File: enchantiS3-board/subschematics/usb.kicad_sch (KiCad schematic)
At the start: 3 parts, among them J1 USB_C_Receptacle_USB2.0, U1 USBLC6-2P6

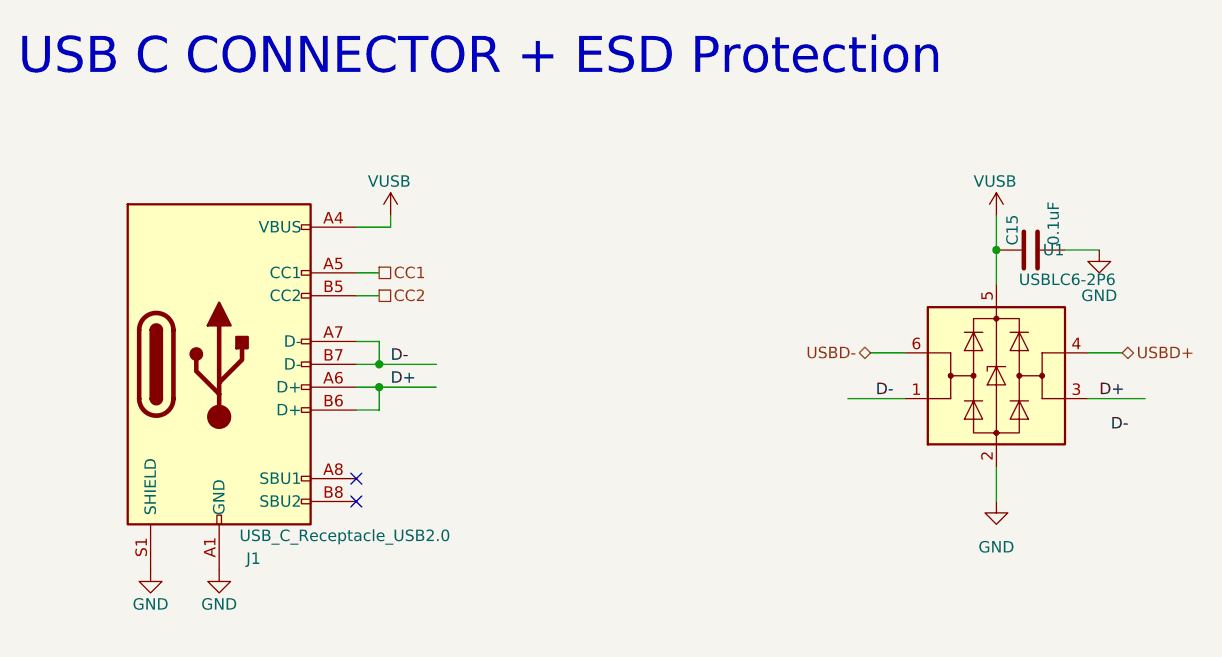
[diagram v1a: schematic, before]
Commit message: Added circuit for magnetometer, added circuit for canfd transceiver, updated circuit for USB connector
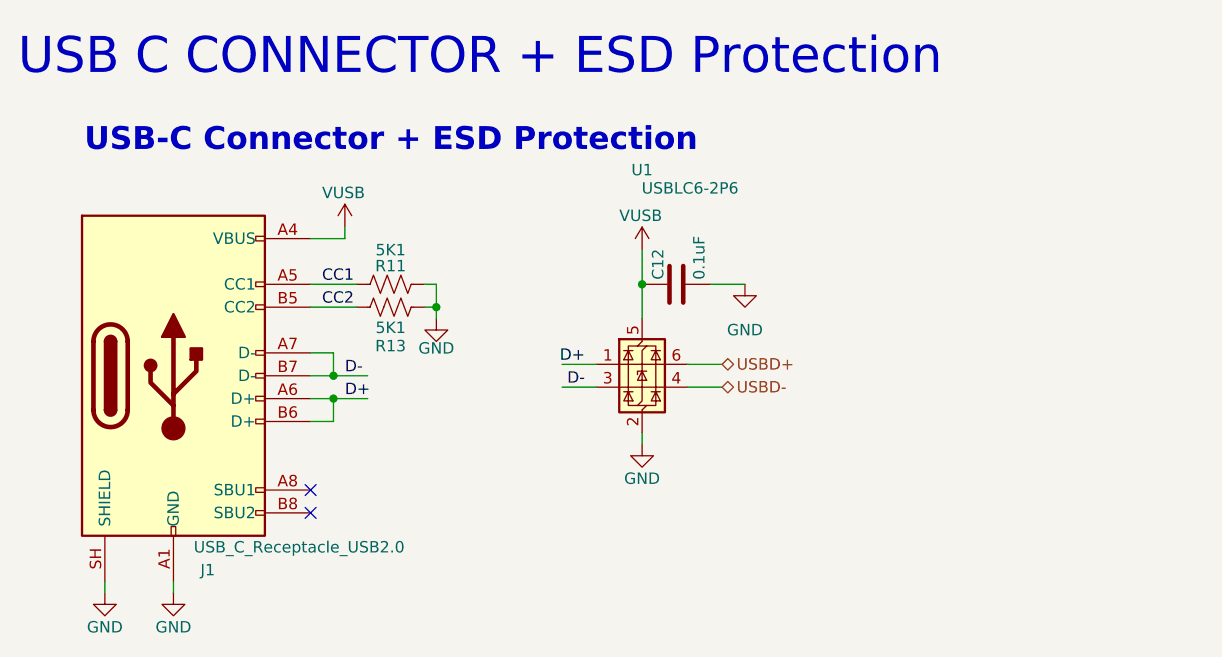
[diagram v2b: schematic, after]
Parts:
- removed C15: 0.1uF, Capacitor_SMD:C_0402_1005Metric, symbol Device:C
- added C12: 0.1uF, Capacitor_SMD:C_0402_1005Metric, symbol Device:C
- added R11, R13: 5K1, Resistor_SMD:R_0402_1005Metric, symbol Device:R_US
- J1: footprint Connector_USB:USB_C_Receptacle_GCT_USB4105-xx-A_16P_TopMnt_Horizontal -> Connector_USB:USB_C_Receptacle_HRO_TYPE-C-31-M-12; symbol Connector:USB_C_Receptacle_USB2.0 -> Connector:USB_C_Receptacle_USB2.0_16P; Manufacturer GCT -> Korean Hroparts Elec; Mfg Part # USB4105-GF-A -> TYPE-C-31-M-12; mpn USB4105-GF-A -> TYPE-C-31-M-12
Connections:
- net CC1: now also R11.1
- net CC2: now also R13.1
- net D+: now also U1.1 (I/O1); no longer U1.3 (I/O2)
- net D-: now also U1.3 (I/O2); no longer U1.1 (I/O1)
- net GND: now also J1.SH (SHIELD), C12.2, R11.2, R13.2; no longer J1.S1 (SHIELD)
- net USBD+: now also U1.6 (I/O1); no longer U1.4 (I/O2)
- net USBD-: now also U1.4 (I/O2); no longer U1.6 (I/O1)
- net VUSB: now also C12.1
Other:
- note added: "USB-C Connector + ESD Protection"
- moved on the sheet: J1
